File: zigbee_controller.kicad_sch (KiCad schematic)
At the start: 75 parts, among them J1 KF635, J10 TerminalBlock_KF301-5.0, J11 TerminalBlock_KF301-5.0, J12 TerminalBlock_KF301-5.0, J13 TerminalBlock_KF301-5.0, J3 Conn_01x06, J4 Conn_01x07, J5 Conn_01x05, P1 USB_C_Receptacle_GCT_USB4105, Q2 IRLB3813, Q3 IRLB3813, Q4 IRLB3813, Q5 IRLB3813, SW2 EN, SW4 Boot, U1 TPS54560, U2 ESP32-C6-MINI-1, U4 TC4427, U5 TC4427, U6 RT9080, U9 CH224K

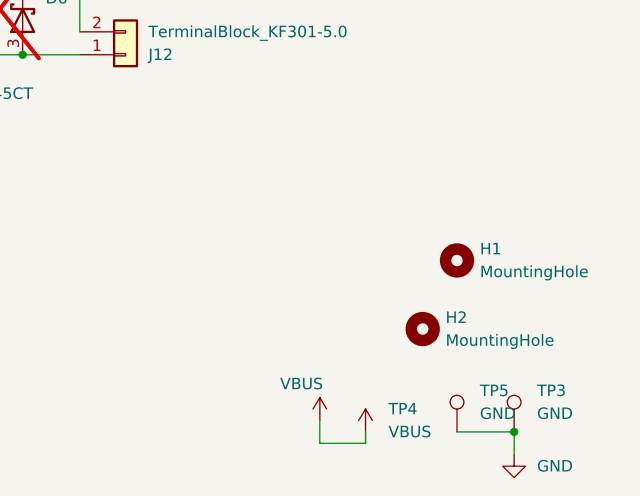
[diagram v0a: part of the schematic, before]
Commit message: Add 3mm holes
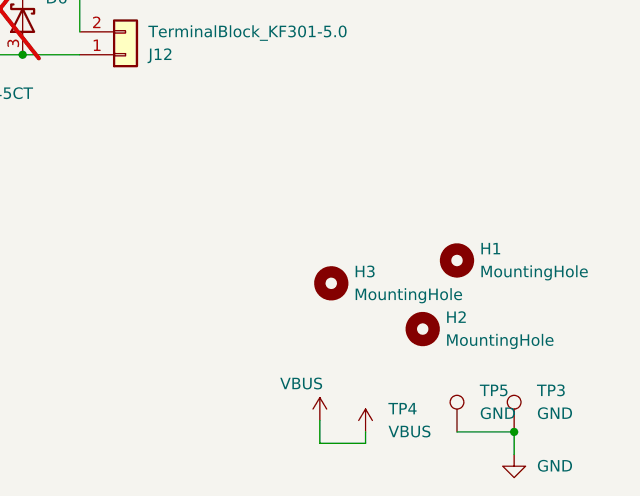
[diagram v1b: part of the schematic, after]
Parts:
- added H3: MountingHole, MountingHole:MountingHole_3mm, symbol Mechanical:MountingHole
- H1, H2: footprint MountingHole:MountingHole_2mm -> MountingHole:MountingHole_3mm
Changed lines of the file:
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@@
 			)
 		)
-		(property "Footprint" "MountingHole:MountingHole_2mm"
+		(property "Footprint" "MountingHole:MountingHole_3mm"
 			(at 373.38 204.47 0)
 			(hide yes)
@@
 	)
 	(symbol
+		(lib_id "Mechanical:MountingHole")
+		(at 363.22 199.39 0)
+		(unit 1)
+		(body_style 1)
+		(exclude_from_sim no)
+		(in_bom no)
+		(on_board yes)
+		(in_pos_files yes)
+		(dnp no)
+		(fields_autoplaced yes)
+		(property "Reference" "H3"
+			(at 365.76 198.1199 0)
+			(show_name no)
+			(do_not_autoplace no)
+			(effects
+				(font
+					(size 1.27 1.27)
+				)
+				(justify left)
+			)
+		)
+		(property "Value" "MountingHole"
+			(at 365.76 200.6599 0)
+			(show_name no)
+			(do_not_autoplace no)
+			(effects
+				(font
+					(size 1.27 1.27)
+				)
+				(justify left)
+			)
+		)
+		(property "Footprint" "MountingHole:MountingHole_3mm"
+			(at 363.22 199.39 0)
+			(hide yes)
+			(show_name no)
+			(do_not_autoplace no)
+			(effects
+				(font
+					(size 1.27 1.27)
+				)
+			)
+		)
+		(property "Datasheet" ""
+			(at 363.22 199.39 0)
+			(hide yes)
+			(show_name no)
+			(do_not_autoplace no)
+			(effects
+				(font
+					(size 1.27 1.27)
+				)
+			)
+		)
+		(property "Description" "Mounting Hole without connection"
+			(at 363.22 199.39 0)
+			(hide yes)
+			(show_name no)
+			(do_not_autoplace no)
+			(effects
+				(font
+					(size 1.27 1.27)
+				)
+			)
+		)
+		(property "in_stock" "-"
+			(at 363.22 199.39 0)
+			(hide yes)
+			(show_name no)
+			(do_not_autoplace no)
+			(effects
+				(font
+					(size 1.27 1.27)
+				)
+			)
+		)
+		(instances
+			(project "zigbee_controller"
+				(path "/17b9f9ac-224d-422f-9c40-54a6770d01d0"
+					(reference "H3")
+					(unit 1)
+				)
+			)
+		)
+	)
+	(symbol
 		(lib_id "Device:D_Schottky_Dual_CommonCathode_AKA_Parallel")
 		(at 326.39 168.91 90)
@@
 			)
 		)
-		(property "Footprint" "MountingHole:MountingHole_2mm"
+		(property "Footprint" "MountingHole:MountingHole_3mm"
 			(at 377.19 196.85 0)
 			(hide yes)

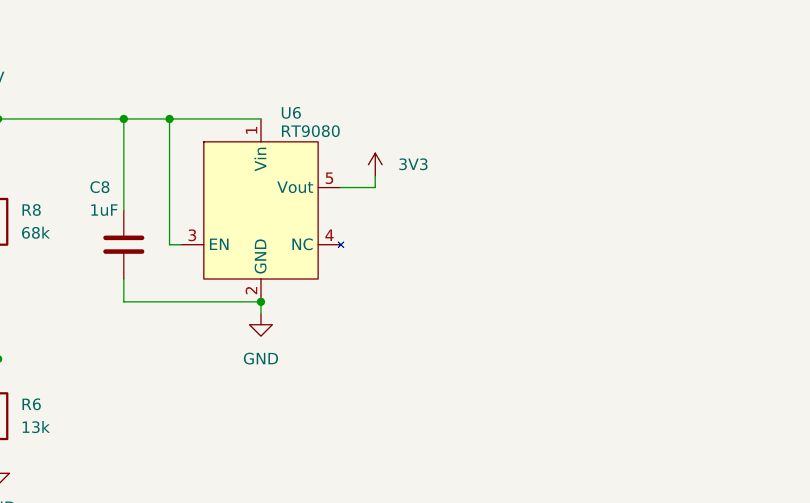
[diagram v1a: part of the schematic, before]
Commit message: Add Output capacitor to RT9080
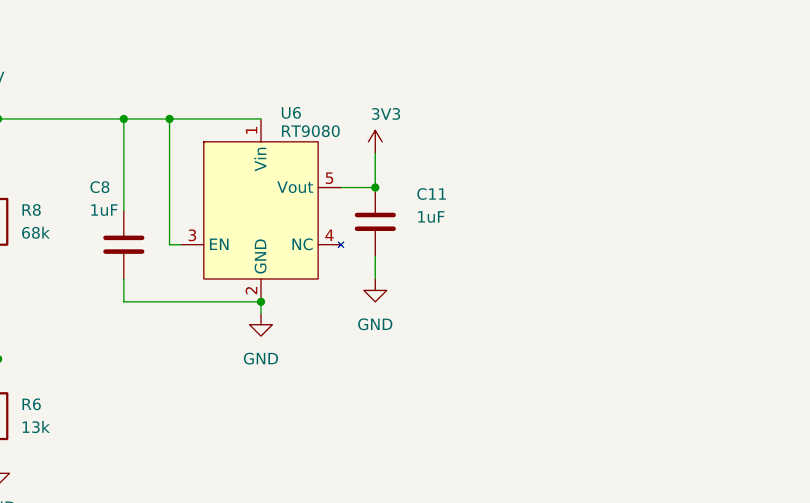
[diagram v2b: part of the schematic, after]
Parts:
- added C11: 1uF, Capacitor_SMD:C_1206_3216Metric, symbol Device:C
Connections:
- net 3V3: now also C11.1
- net GND: now also C11.2
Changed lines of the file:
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@@
 	)
 	(junction
+		(at 278.13 31.75)
+		(diameter 0)
+		(color 0 0 0 0)
+	)
+	(junction
 		(at 262.89 158.75)
 		(diameter 0)
@@
 	(wire
 		(pts
-			(xy 278.13 30.48) (xy 278.13 31.75)
+			(xy 278.13 27.94) (xy 278.13 31.75)
 		)
 		(stroke
@@
 	(wire
 		(pts
+			(xy 278.13 41.91) (xy 278.13 39.37)
+		)
+		(stroke
+			(width 0)
+			(type default)
+		)
+	)
+	(wire
+		(pts
 			(xy 114.3 160.02) (xy 123.19 160.02)
 		)
@@
 	(symbol
 		(lib_id "power:+3.3V")
-		(at 278.13 30.48 0)
+		(at 278.13 27.94 0)
 		(unit 1)
 		(body_style 1)
@@
 		(in_pos_files yes)
 		(dnp no)
-		(fields_autoplaced yes)
 		(property "Reference" "#PWR043"
-			(at 278.13 34.29 0)
+			(at 278.13 31.75 0)
 			(hide yes)
 			(show_name no)
@@
 		)
 		(property "Value" "3V3"
-			(at 280.67 29.2099 0)
+			(at 277.622 23.622 0)
 			(show_name no)
 			(do_not_autoplace no)
@@
 		)
 		(property "Footprint" ""
-			(at 278.13 30.48 0)
+			(at 278.13 27.94 0)
 			(hide yes)
 			(show_name no)
@@
 		)
 		(property "Datasheet" ""
-			(at 278.13 30.48 0)
+			(at 278.13 27.94 0)
 			(hide yes)
 			(show_name no)
@@
 		)
 		(property "Description" "Power symbol creates a global label with name \"+3.3V\""
-			(at 278.13 30.48 0)
+			(at 278.13 27.94 0)
 			(hide yes)
 			(show_name no)
@@
 	)
 	(symbol
+		(lib_id "Device:C")
+		(at 278.13 35.56 0)
+		(unit 1)
+		(body_style 1)
+		(exclude_from_sim no)
+		(in_bom yes)
+		(on_board yes)
+		(in_pos_files yes)
+		(dnp no)
+		(property "Reference" "C11"
+			(at 282.702 32.512 0)
+			(show_name no)
+			(do_not_autoplace no)
+			(effects
+				(font
+					(size 1.27 1.27)
+				)
+				(justify left)
+			)
+		)
+		(property "Value" "1uF"
+			(at 282.702 35.052 0)
+			(show_name no)
+			(do_not_autoplace no)
+			(effects
+				(font
+					(size 1.27 1.27)
+				)
+				(justify left)
+			)
+		)
+		(property "Footprint" "Capacitor_SMD:C_1206_3216Metric"
+			(at 279.0952 39.37 0)
+			(hide yes)
+			(show_name no)
+			(do_not_autoplace no)
+			(effects
+				(font
+					(size 1.27 1.27)
+				)
+			)
+		)
+		(property "Datasheet" ""
+			(at 278.13 35.56 0)
+			(hide yes)
+			(show_name no)
+			(do_not_autoplace no)
+			(effects
+				(font
+					(size 1.27 1.27)
+				)
+			)
+		)
+		(property "Description" "Unpolarized capacitor"
+			(at 278.13 35.56 0)
+			(hide yes)
+			(show_name no)
+			(do_not_autoplace no)
+			(effects
+				(font
+					(size 1.27 1.27)
+				)
+			)
+		)
+		(property "in_stock" "yes"
+			(at 278.13 35.56 0)
+			(hide yes)
+			(show_name no)
+			(do_not_autoplace no)
+			(effects
+				(font
+					(size 1.27 1.27)
+				)
+			)
+		)
+		(pin "1"
+		)
+		(pin "2"
+		)
+		(instances
+			(project "zigbee_controller"
+				(path "/17b9f9ac-224d-422f-9c40-54a6770d01d0"
+					(reference "C11")
+					(unit 1)
+				)
+			)
+		)
+	)
+	(symbol
 		(lib_id "Transistor_FET:IRLB8721PBF")
 		(at 271.78 156.21 270)
@@
 					(unit 1)
 				)
+			)
+		)
+	)
+	(symbol
+		(lib_id "power:GND")
+		(at 278.13 41.91 0)
+		(unit 1)
+		(body_style 1)
+		(exclude_from_sim no)
+		(in_bom yes)
+		(on_board yes)
+		(in_pos_files yes)
+		(dnp no)
+		(fields_autoplaced yes)
+		(property "Reference" "#PWR049"
+			(at 278.13 48.26 0)
+			(hide yes)
+			(show_name no)
+			(do_not_autoplace no)
+			(effects
+				(font
+					(size 1.27 1.27)
+				)
+			)
+		)
+		(property "Value" "GND"
+			(at 278.13 46.99 0)
+			(show_name no)
+			(do_not_autoplace no)
+			(effects
+				(font
+					(size 1.27 1.27)
+				)
+			)
+		)
+		(property "Footprint" ""
+			(at 278.13 41.91 0)
+			(hide yes)
+			(show_name no)
+			(do_not_autoplace no)
+			(effects
+				(font
+					(size 1.27 1.27)
+				)
+			)
+		)
+		(property "Datasheet" ""
+			(at 278.13 41.91 0)
+			(hide yes)
+			(show_name no)
+			(do_not_autoplace no)
+			(effects
+				(font
+					(size 1.27 1.27)
+				)
+			)
+		)
+		(property "Description" "Power symbol creates a global label with name \"GND\" , ground"
+			(at 278.13 41.91 0)
+			(hide yes)
+			(show_name no)
+			(do_not_autoplace no)
+			(effects
+				(font
+					(size 1.27 1.27)
+				)
+			)
+		)
+		(pin "1"
+		)
+		(instances
+			(project "zigbee_controller"
+				(path "/17b9f9ac-224d-422f-9c40-54a6770d01d0"
+					(reference "#PWR049")
+					(unit 1)
+				)

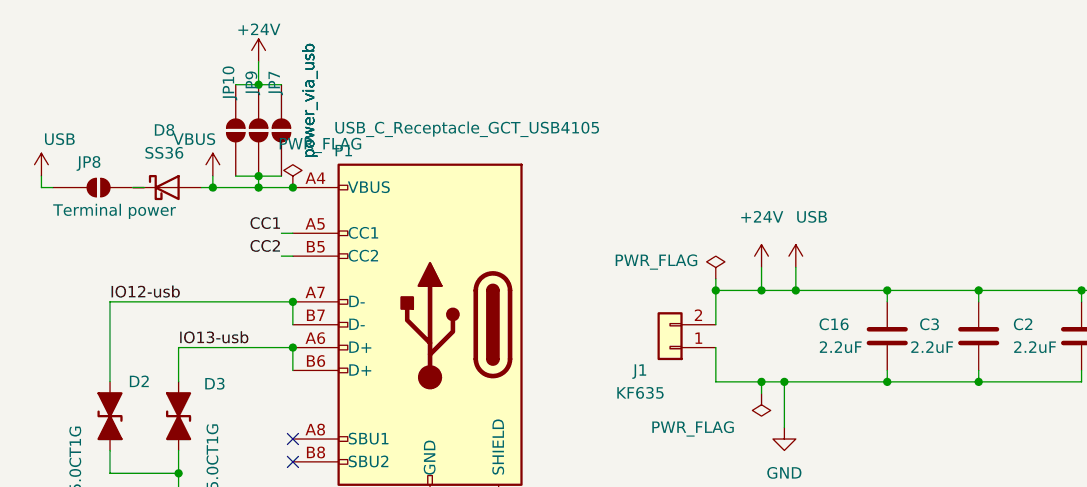
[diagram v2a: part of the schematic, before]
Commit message: two diods for USB powering when in terminal mode
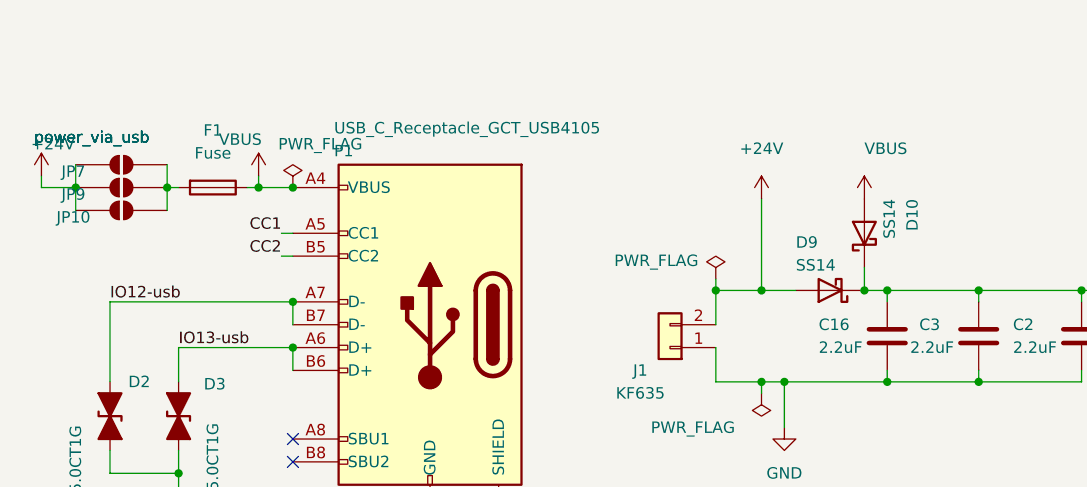
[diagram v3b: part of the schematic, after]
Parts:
- removed D8: SS36, Diode_SMD:D_SMA, symbol Diode:SS36
- removed JP8: Terminal power, Jumper:SolderJumper-2_P1.3mm_Open_RoundedPad1.0x1.5mm, symbol Jumper:SolderJumper_2_Open
- added D10, D9: SS14, Diode_SMD:D_SMA, symbol Diode:SS14
- added F1: Fuse, Fuse:Fuse_1206_3216Metric, symbol Device:Fuse
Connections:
- net +24V: now also D9.2 (A); no longer C16.1, C2.1, C3.1, U1.2 (VIN)
- net VBUS: now also D10.2 (A), F1.1; no longer JP10.2 (B), JP7.2 (B), JP9.2 (B)
- new net: F1.2, JP10.2 (B), JP7.2 (B), JP9.2 (B)
- new net: C16.1, C2.1, C3.1, D10.1 (K), D9.1 (K), U1.2 (VIN)
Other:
- moved on the sheet: JP10, JP7, JP9

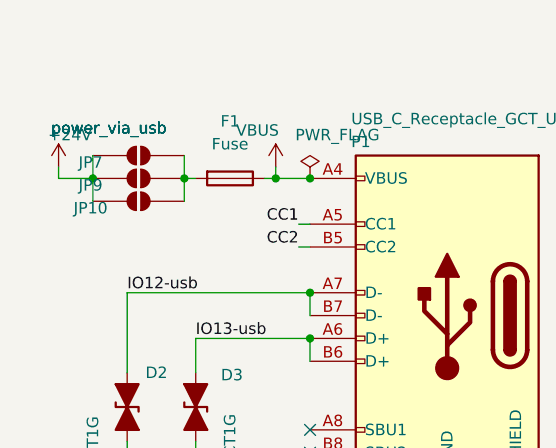
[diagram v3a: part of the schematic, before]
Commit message: USB powering via 3A or 5A fuse
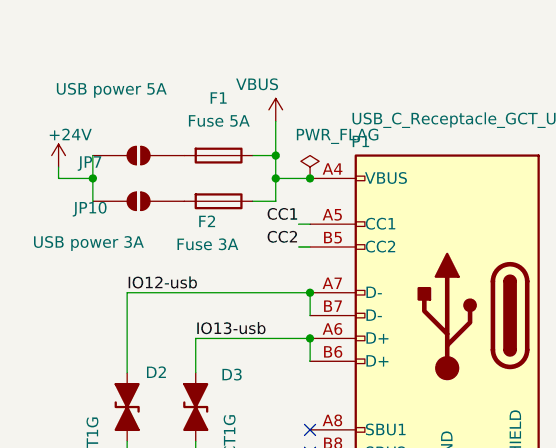
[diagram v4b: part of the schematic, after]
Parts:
- removed JP9: power_via_usb, Jumper:SolderJumper-2_P1.3mm_Open_RoundedPad1.0x1.5mm, symbol Jumper:SolderJumper_2_Open
- added F2: Fuse 3A, Fuse:Fuse_1206_3216Metric, symbol Device:Fuse
- F1: value Fuse -> Fuse 5A
- JP10: value power_via_usb -> USB power 3A
- JP7: value power_via_usb -> USB power 5A
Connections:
- net VBUS: now also F2.1
- net at F1.2, JP7.2 (B): no longer JP10.2 (B)
- new net: F2.2, JP10.2 (B)

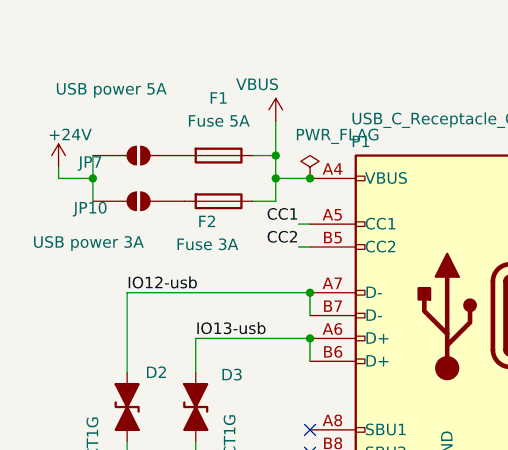
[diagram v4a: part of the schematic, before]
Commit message: Double pads for USB power
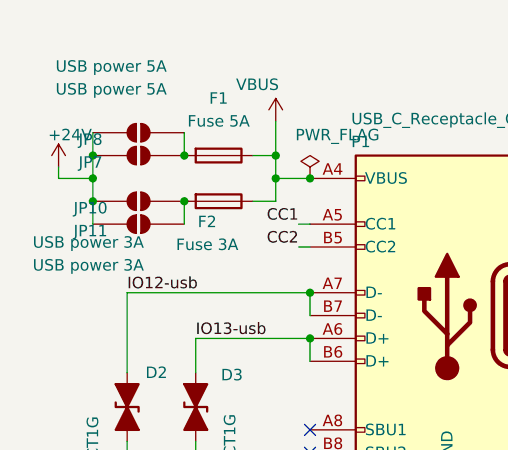
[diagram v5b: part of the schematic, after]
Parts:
- added JP11: USB power 3A, Jumper:SolderJumper-2_P1.3mm_Open_RoundedPad1.0x1.5mm, symbol Jumper:SolderJumper_2_Open
- added JP8: USB power 5A, Jumper:SolderJumper-2_P1.3mm_Open_RoundedPad1.0x1.5mm, symbol Jumper:SolderJumper_2_Open
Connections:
- net +24V: now also JP11.1 (A), JP8.1 (A)
- net at F1.2, JP7.2 (B): now also JP8.2 (B)
- net at F2.2, JP10.2 (B): now also JP11.2 (B)
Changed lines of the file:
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@@
 	)
 	(junction
+		(at 27.94 34.29)
+		(diameter 0)
+		(color 0 0 0 0)
+	)
+	(junction
 		(at 328.93 173.99)
 		(diameter 0)
@@
 	)
 	(junction
+		(at 27.94 29.21)
+		(diameter 0)
+		(color 0 0 0 0)
+	)
+	(junction
 		(at 326.39 161.29)
 		(diameter 0)
@@
 	)
 	(junction
+		(at 17.78 34.29)
+		(diameter 0)
+		(color 0 0 0 0)
+	)
+	(junction
 		(at 176.53 160.02)
 		(diameter 0)
@@
 	)
 	(junction
+		(at 17.78 29.21)
+		(diameter 0)
+		(color 0 0 0 0)
+	)
+	(junction
 		(at 200.66 162.56)
 		(diameter 0)
@@
 	(wire
 		(pts
+			(xy 27.94 26.67) (xy 27.94 29.21)
+		)
+		(stroke
+			(width 0)
+			(type default)
+		)
+	)
+	(wire
+		(pts
 			(xy 118.11 44.45) (xy 118.11 43.18)
 		)
@@
 	(wire
 		(pts
+			(xy 17.78 26.67) (xy 17.78 29.21)
+		)
+		(stroke
+			(width 0)
+			(type default)
+		)
+	)
+	(wire
+		(pts
 			(xy 88.9 49.53) (xy 88.9 53.34)
 		)
@@
 	(wire
 		(pts
+			(xy 27.94 34.29) (xy 27.94 36.83)
+		)
+		(stroke
+			(width 0)
+			(type default)
+		)
+	)
+	(wire
+		(pts
 			(xy 20.32 120.65) (xy 20.32 118.11)
 		)
@@
 	(wire
 		(pts
+			(xy 17.78 34.29) (xy 17.78 36.83)
+		)
+		(stroke
+			(width 0)
+			(type default)
+		)
+	)
+	(wire
+		(pts
 			(xy 236.22 24.13) (xy 250.19 24.13)
 		)
@@
 	)
 	(symbol
+		(lib_id "Jumper:SolderJumper_2_Open")
+		(at 22.86 36.83 0)
+		(unit 1)
+		(body_style 1)
+		(exclude_from_sim no)
+		(in_bom no)
+		(on_board yes)
+		(in_pos_files yes)
+		(dnp no)
+		(property "Reference" "JP11"
+			(at 17.526 37.592 0)
+			(show_name no)
+			(do_not_autoplace no)
+			(effects
+				(font
+					(size 1.27 1.27)
+				)
+			)
+		)
+		(property "Value" "USB power 3A"
+			(at 17.272 41.402 0)
+			(show_name no)
+			(do_not_autoplace no)
+			(effects
+				(font
+					(size 1.27 1.27)
+				)
+			)
+		)
+		(property "Footprint" "Jumper:SolderJumper-2_P1.3mm_Open_RoundedPad1.0x1.5mm"
+			(at 22.86 36.83 0)
+			(hide yes)
+			(show_name no)
+			(do_not_autoplace no)
+			(effects
+				(font
+					(size 1.27 1.27)
+				)
+			)
+		)
+		(property "Datasheet" ""
+			(at 22.86 44.45 0)
+			(hide yes)
+			(show_name no)
+			(do_not_autoplace no)
+			(effects
+				(font
+					(size 1.27 1.27)
+				)
+			)
+		)
+		(property "Description" "Solder Jumper, 2-pole, open"
+			(at 22.86 41.91 0)
+			(hide yes)
+			(show_name no)
+			(do_not_autoplace no)
+			(effects
+				(font
+					(size 1.27 1.27)
+				)
+			)
+		)
+		(property "in_stock" "-"
+			(at 22.86 36.83 0)
+			(hide yes)
+			(show_name no)
+			(do_not_autoplace no)
+			(effects
+				(font
+					(size 1.27 1.27)
+				)
+			)
+		)
+		(pin "2"
+		)
+		(pin "1"
+		)
+		(instances
+			(project "zigbee_controller"
+				(path "/17b9f9ac-224d-422f-9c40-54a6770d01d0"
+					(reference "JP11")
+					(unit 1)
+				)
+			)
+		)
+	)
+	(symbol
 		(lib_id "Device:D_Schottky_Dual_CommonCathode_AKA_Parallel")
 		(at 200.66 170.18 90)
@@
 					(unit 1)
 				)
+			)
+		)
+	)
+	(symbol
+		(lib_id "Jumper:SolderJumper_2_Open")
+		(at 22.86 26.67 0)
+		(unit 1)
+		(body_style 1)
+		(exclude_from_sim no)
+		(in_bom no)
+		(on_board yes)
+		(in_pos_files yes)
+		(dnp no)
+		(property "Reference" "JP8"
+			(at 17.526 27.432 0)
+			(show_name no)
+			(do_not_autoplace no)
+			(effects
+				(font
+					(size 1.27 1.27)
+				)
+			)
+		)
+		(property "Value" "USB power 5A"
+			(at 19.812 19.304 0)
+			(show_name no)
+			(do_not_autoplace no)
+			(effects
+				(font
+					(size 1.27 1.27)
+				)
+			)
+		)
+		(property "Footprint" "Jumper:SolderJumper-2_P1.3mm_Open_RoundedPad1.0x1.5mm"
+			(at 22.86 26.67 0)
+			(hide yes)
+			(show_name no)
+			(do_not_autoplace no)
+			(effects
+				(font
+					(size 1.27 1.27)
+				)
+			)
+		)
+		(property "Datasheet" ""
+			(at 22.86 34.29 0)
+			(hide yes)
+			(show_name no)
+			(do_not_autoplace no)
+			(effects
+				(font
+					(size 1.27 1.27)
+				)
+			)
+		)
+		(property "Description" "Solder Jumper, 2-pole, open"
+			(at 22.86 31.75 0)
+			(hide yes)
+			(show_name no)
+			(do_not_autoplace no)
+			(effects
+				(font
+					(size 1.27 1.27)
+				)
+			)
+		)
+		(property "in_stock" "-"
+			(at 22.86 26.67 0)
+			(hide yes)
+			(show_name no)
+			(do_not_autoplace no)
+			(effects
+				(font
+					(size 1.27 1.27)
+				)
+			)
+		)
+		(pin "2"
+		)
+		(pin "1"
+		)
+		(instances
+			(project "zigbee_controller"
+				(path "/17b9f9ac-224d-422f-9c40-54a6770d01d0"
+					(reference "JP8")
+					(unit 1)
+				)
